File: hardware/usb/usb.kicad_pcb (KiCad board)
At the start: 2 copper layers, 27.5 x 17.6 mm, 17 parts, among them J1 Conn_01x04, J2 Conn_01x02, J3 Conn_01x02, J4 Conn_01x01, J5 Conn_01x02, J6 Conn_01x01, J7 Conn_01x01, J8 Conn_01x01, U1 USBLC6-2SC6, U2 AMS1117-3.3

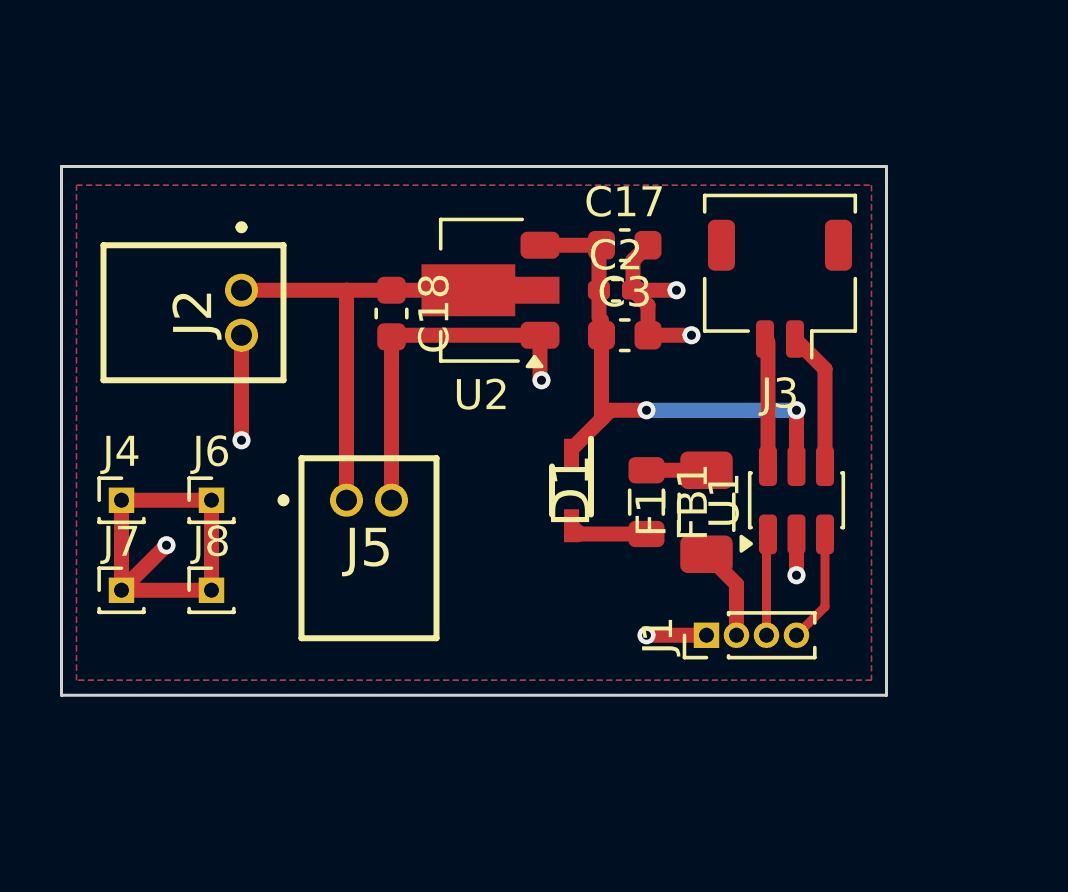
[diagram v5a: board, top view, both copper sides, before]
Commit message: fix usb connectors
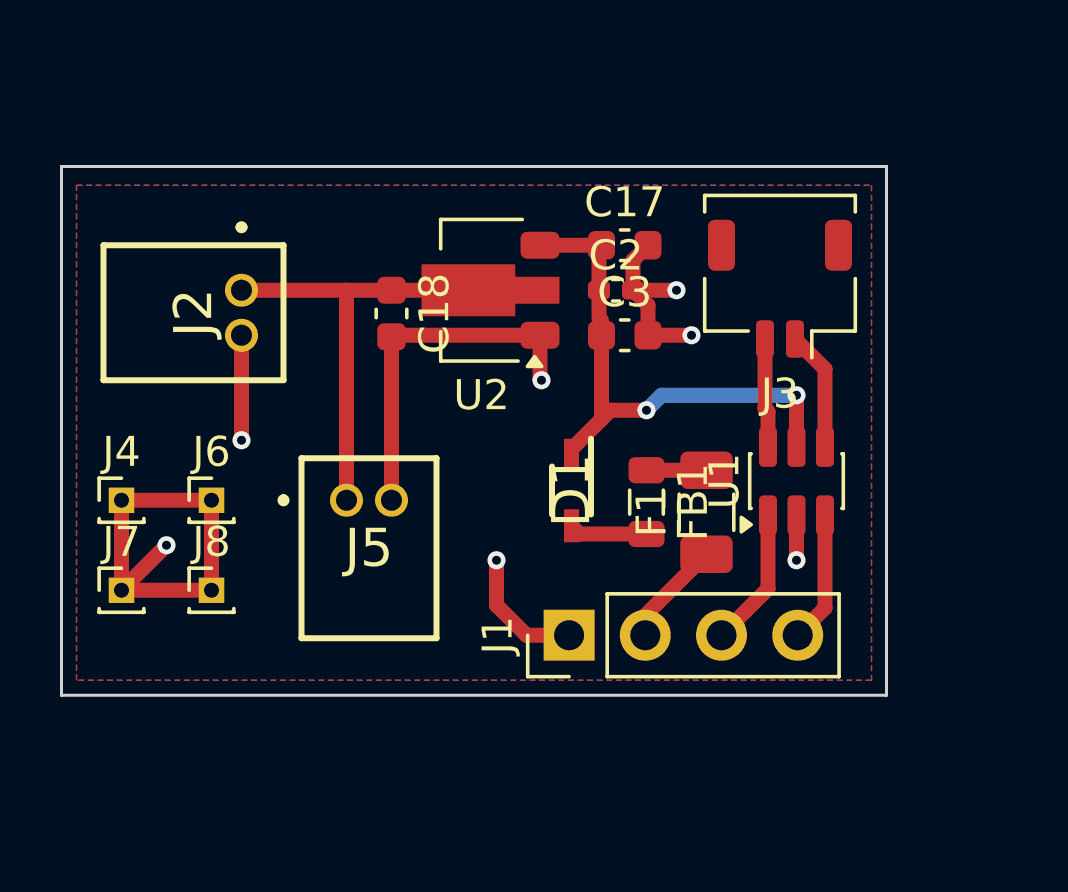
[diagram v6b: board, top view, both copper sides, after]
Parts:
- J1: footprint Connector_PinHeader_1.00mm:PinHeader_1x04_P1.00mm_Vertical -> Connector_PinHeader_2.54mm:PinHeader_1x04_P2.54mm_Vertical
- moved J1 4.58 mm to (106.4, 80.5)
- moved U1 0.64 mm to (114.0, 75.4)
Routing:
- net GND: track 38.7 -> 41.2 mm
- net /D-: track 3.38 -> 4.64 mm
- net Net-(J3-Pin_1): track 4.65 -> 4.01 mm
- net /D+: track 3.83 -> 4.38 mm
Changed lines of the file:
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@@
 	(footprint "Package_TO_SOT_SMD:SOT-23-6"
 		(layer "F.Cu")
-		(at 114 76 90)
+		(at 114 75.3625 90)
 		(descr "SOT, 6 Pin (JEDEC MO-178 Var AB https://www.jedec.org/document_search?search_api_views_fulltext=MO-178), generated with kicad-footprint-generator ipc_gullwing_generator.py")
 		(tags "SOT TO_SOT_SMD")
@@
 		)
 	)
-	(footprint "Connector_PinHeader_1.00mm:PinHeader_1x04_P1.00mm_Vertical"
+	(footprint "Connector_PinHeader_2.54mm:PinHeader_1x04_P2.54mm_Vertical"
 		(layer "F.Cu")
-		(at 111 80.5 90)
-		(descr "Through hole straight pin header, 1x04, 1.00mm pitch, single row")
-		(tags "Through hole pin header THT 1x04 1.00mm single row")
+		(at 106.42 80.5 90)
+		(descr "Through hole straight pin header, 1x04, 2.54mm pitch, single row")
+		(tags "Through hole pin header THT 1x04 2.54mm single row")
 		(property "Reference" "J1"
-			(at 0 -1.61 90)
+			(at 0 -2.38 90)
 			(layer "F.SilkS")
 			(effects
@@
 		)
 		(property "Value" "Conn_01x04"
-			(at 0 4.61 90)
+			(at 0 10 90)
 			(layer "F.Fab")
 			(effects
@@
 		(attr through_hole)
 		(fp_line
-			(start -0.745 -0.735)
-			(end 0 -0.735)
+			(start -1.38 -1.38)
+			(end 0 -1.38)
 			(stroke
 				(width 0.12)
@@
 		)
 		(fp_line
-			(start -0.745 0)
-			(end -0.745 -0.735)
+			(start -1.38 0)
+			(end -1.38 -1.38)
 			(stroke
 				(width 0.12)
@@
 		)
 		(fp_line
-			(start 0.745 0.735)
-			(end 0.745 3.61)
+			(start 1.38 1.27)
+			(end 1.38 9)
 			(stroke
 				(width 0.12)
@@
 		)
 		(fp_line
-			(start 0.685565 0.735)
-			(end 0.745 0.735)
+			(start -1.38 1.27)
+			(end 1.38 1.27)
 			(stroke
 				(width 0.12)
@@
 		)
 		(fp_line
-			(start -0.745 0.735)
-			(end -0.685565 0.735)
+			(start -1.38 1.27)
+			(end -1.38 9)
 			(stroke
 				(width 0.12)
@@
 		)
 		(fp_line
-			(start -0.745 0.735)
-			(end -0.745 3.61)
-			(stroke
-				(width 0.12)
-				(type solid)
-			)
-			(layer "F.SilkS")
-		)
-		(fp_line
-			(start 0.41003 3.61)
-			(end 0.745 3.61)
-			(stroke
-				(width 0.12)
-				(type solid)
-			)
-			(layer "F.SilkS")
-		)
-		(fp_line
-			(start -0.745 3.61)
-			(end -0.41003 3.61)
+			(start -1.38 9)
+			(end 1.38 9)
 			(stroke
 				(width 0.12)
@@
 		)
 		(fp_rect
-			(start -1.14 -1)
-			(end 1.14 4)
+			(start -1.77 -1.77)
+			(end 1.77 9.39)
 			(stroke
 				(width 0.05)
@@
 		)
 		(fp_line
-			(start 0.635 -0.5)
-			(end 0.635 3.5)
+			(start 1.27 -1.27)
+			(end 1.27 8.89)
 			(stroke
 				(width 0.1)
@@
 		)
 		(fp_line
-			(start -0.3175 -0.5)
-			(end 0.635 -0.5)
+			(start -0.635 -1.27)
+			(end 1.27 -1.27)
 			(stroke
 				(width 0.1)
@@
 		)
 		(fp_line
-			(start -0.635 -0.1825)
-			(end -0.3175 -0.5)
+			(start -1.27 -0.635)
+			(end -0.635 -1.27)
 			(stroke
 				(width 0.1)
@@
 		)
 		(fp_line
-			(start 0.635 3.5)
-			(end -0.635 3.5)
+			(start 1.27 8.89)
+			(end -1.27 8.89)
 			(stroke
 				(width 0.1)
@@
 		)
 		(fp_line
-			(start -0.635 3.5)
-			(end -0.635 -0.1825)
+			(start -1.27 8.89)
+			(end -1.27 -0.635)
 			(stroke
 				(width 0.1)
@@
 		)
 		(fp_text user "${REFERENCE}"
-			(at 0 1.5 0)
+			(at 0 3.81 180)
 			(layer "F.Fab")
 			(effects
 				(font
-					(size 0.76 0.76)
-					(thickness 0.114)
+					(size 1 1)
+					(thickness 0.15)
 				)
 			)
@@
 		(pad "1" thru_hole rect
 			(at 0 0 90)
-			(size 0.85 0.85)
-			(drill 0.5)
+			(size 1.7 1.7)
+			(drill 1)
 			(layers "*.Cu" "*.Mask")
 			(remove_unused_layers no)
@@
 		)
 		(pad "2" thru_hole circle
-			(at 0 1 90)
-			(size 0.85 0.85)
-			(drill 0.5)
+			(at 0 2.54 90)
+			(size 1.7 1.7)
+			(drill 1)
 			(layers "*.Cu" "*.Mask")
 			(remove_unused_layers no)
@@
 		)
 		(pad "3" thru_hole circle
-			(at 0 2 90)
-			(size 0.85 0.85)
-			(drill 0.5)
+			(at 0 5.08 90)
+			(size 1.7 1.7)
+			(drill 1)
 			(layers "*.Cu" "*.Mask")
 			(remove_unused_layers no)
@@
 		)
 		(pad "4" thru_hole circle
-			(at 0 3 90)
-			(size 0.85 0.85)
-			(drill 0.5)
+			(at 0 7.62 90)
+			(size 1.7 1.7)
+			(drill 1)
 			(layers "*.Cu" "*.Mask")
 			(remove_unused_layers no)
@@
 		)
 		(embedded_fonts no)
-		(model "${KICAD9_3DMODEL_DIR}/Connector_PinHeader_1.00mm.3dshapes/PinHeader_1x04_P1.00mm_Vertical.step"
+		(model "${KICAD9_3DMODEL_DIR}/Connector_PinHeader_2.54mm.3dshapes/PinHeader_1x04_P2.54mm_Vertical.step"
 			(offset
 				(xyz 0 0 0)
@@
 	)
 	(segment
-		(start 111 80.5)
-		(end 109 80.5)
+		(start 91.5 79)
+		(end 93 77.5)
 		(width 0.5)
 		(layer "F.Cu")
@@
 	)
 	(segment
-		(start 91.5 79)
-		(end 93 77.5)
+		(start 109.05 69.5)
+		(end 108.55 69)
 		(width 0.5)
 		(layer "F.Cu")
@@
 	)
 	(segment
-		(start 109.05 69.5)
-		(end 108.55 69)
+		(start 105 80.5)
+		(end 104 79.5)
 		(width 0.5)
 		(layer "F.Cu")
@@
 	)
 	(segment
-		(start 114 77.1375)
-		(end 114 78.5)
+		(start 109.05 70.5)
+		(end 110.5 70.5)
 		(width 0.5)
 		(layer "F.Cu")
@@
 	)
 	(segment
-		(start 109.05 70.5)
-		(end 110.5 70.5)
+		(start 104 79.5)
+		(end 104 78)
+		(width 0.5)
+		(layer "F.Cu")
+		(net 1)
+	)
+	(segment
+		(start 114 78)
+		(end 114 76.5)
 		(width 0.5)
 		(layer "F.Cu")
@@
 	)
 	(segment
+		(start 106.42 80.5)
+		(end 105 80.5)
+		(width 0.5)
+		(layer "F.Cu")
+		(net 1)
+	)
+	(segment
 		(start 94.5 76)
 		(end 94.5 79)
@@
 	)
 	(via
-		(at 109 80.5)
+		(at 104 78)
 		(size 0.604799)
 		(drill 0.299999)
@@
 	)
 	(via
-		(at 114 78.5)
+		(at 114 78)
 		(size 0.604799)
 		(drill 0.299999)
@@
 	)
 	(segment
-		(start 113.05 74.8625)
-		(end 113.05 70.725)
+		(start 113.05 74.225)
+		(end 113.05 73.05)
+		(width 0.5)
+		(layer "F.Cu")
+		(net 2)
+	)
+	(segment
+		(start 112.95 72.95)
+		(end 112.95 70.625)
+		(width 0.5)
+		(layer "F.Cu")
+		(net 2)
+	)
+	(segment
+		(start 113.05 73.05)
+		(end 112.95 72.95)
 		(width 0.5)
 		(layer "F.Cu")
@@
 	)
 	(segment
-		(start 114.95 71.625)
-		(end 113.95 70.625)
+		(start 114.95 74.225)
+		(end 114.95 71.625)
 		(width 0.5)
 		(layer "F.Cu")
@@
 	)
 	(segment
-		(start 114.95 74.8625)
-		(end 114.95 71.625)
+		(start 114.95 71.625)
+		(end 113.95 70.625)
 		(width 0.5)
 		(layer "F.Cu")
@@
 	)
 	(segment
+		(start 114 74.225)
+		(end 114 72.5)
+		(width 0.5)
+		(layer "F.Cu")
+		(net 6)
+	)
+	(segment
 		(start 107.415 69.915)
 		(end 107.415 69)
@@
 	)
 	(segment
-		(start 114 74.8625)
-		(end 114 73)
-		(width 0.5)
-		(layer "F.Cu")
-		(net 6)
-	)
-	(segment
 		(start 106.5 74.3)
 		(end 107.5 73.3)
@@
 	)
 	(via
-		(at 114 73)
+		(at 114 72.5)
 		(size 0.604799)
 		(drill 0.299999)
@@
 	)
 	(segment
-		(start 114 73)
-		(end 109 73)
+		(start 109.5 72.5)
+		(end 114 72.5)
+		(width 0.5)
+		(layer "B.Cu")
+		(net 6)
+	)
+	(segment
+		(start 109 73)
+		(end 109.5 72.5)
 		(width 0.5)
 		(layer "B.Cu")
@@
 	)
 	(segment
-		(start 113 80.5)
-		(end 113 77.1875)
-		(width 0.3)
+		(start 111.5 80.5)
+		(end 113.05 78.95)
+		(width 0.5)
 		(layer "F.Cu")
 		(net 8)
 	)
 	(segment
-		(start 113 77.1875)
-		(end 113.05 77.1375)
-		(width 0.155814)
+		(start 113.05 78.95)
+		(end 113.05 76.5)
+		(width 0.5)
 		(layer "F.Cu")
 		(net 8)
 	)
 	(segment
-		(start 114.95 79.55)
-		(end 114.95 77.1375)
-		(width 0.3)
-		(layer "F.Cu")
-		(net 9)
-	)
-	(segment
-		(start 114 80.5)
-		(end 114.95 79.55)
-		(width 0.3)
+		(start 114.95 79.59)
+		(end 114.95 76.5)
+		(width 0.5)
 		(layer "F.Cu")
 		(net 9)
 	)
 	(segment
-		(start 115 77.1875)
-		(end 114.95 77.1375)
-		(width 0.155814)
+		(start 114.04 80.5)
+		(end 114.95 79.59)
+		(width 0.5)
 		(layer "F.Cu")
 		(net 9)
 	)
 	(segment
-		(start 112 78.8)
+		(start 108.96 79.84)
 		(end 111 77.8)
 		(width 0.5)
@@
 	)
 	(segment
-		(start 112 80.5)
-		(end 112 78.8)
-		(width 0.5)
+		(start 108.96 80.5)
+		(end 108.96 79.84)
+		(width 0.1524)
 		(layer "F.Cu")
 		(net 10)
